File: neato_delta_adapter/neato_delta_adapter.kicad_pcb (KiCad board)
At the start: 2 copper layers, 43 x 21 mm, 11 parts, among them J1 JST PH2.0 B4B Vert, J2 JST PH2.0 B2B Vert, J3 JST PH B4B Vert, J4 JST PH2.0 B5B Vert, Q1 AS2302, U1 DNP LM2596

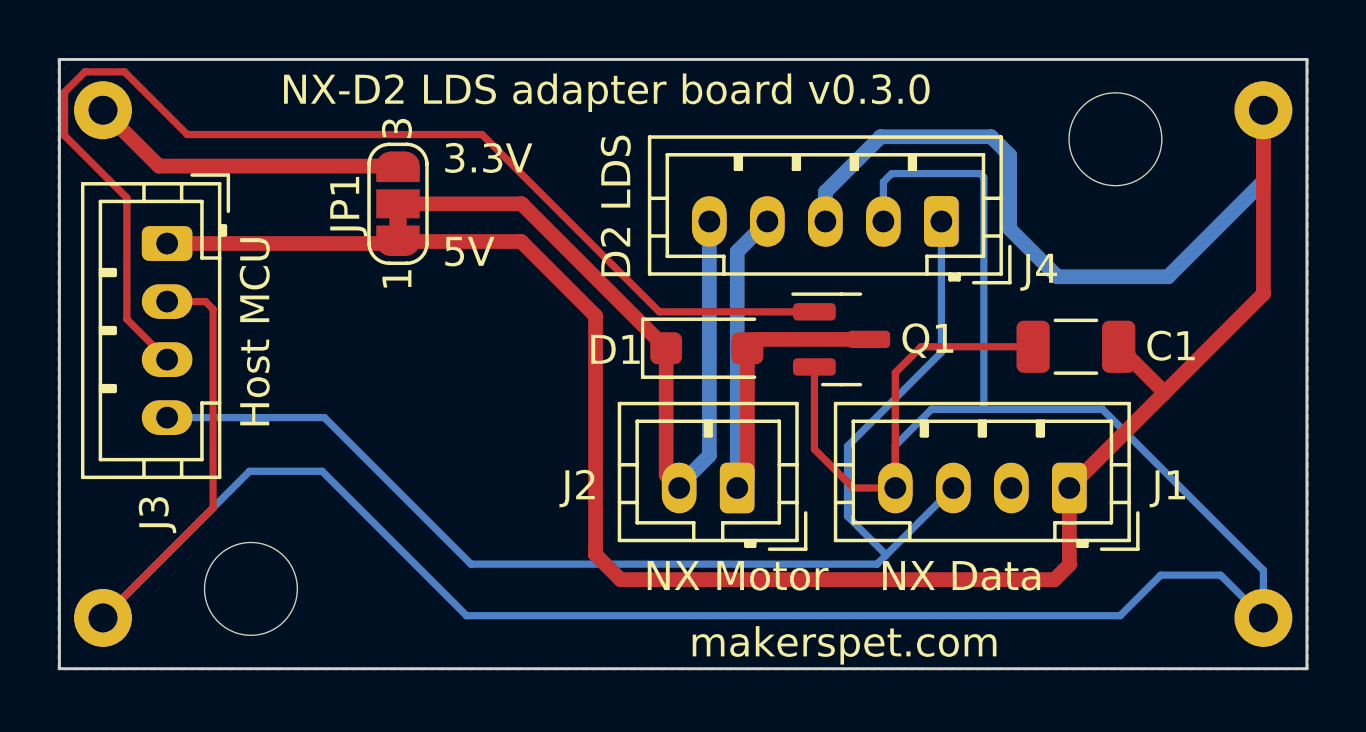
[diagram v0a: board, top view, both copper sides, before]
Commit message: Level shifter for Delta
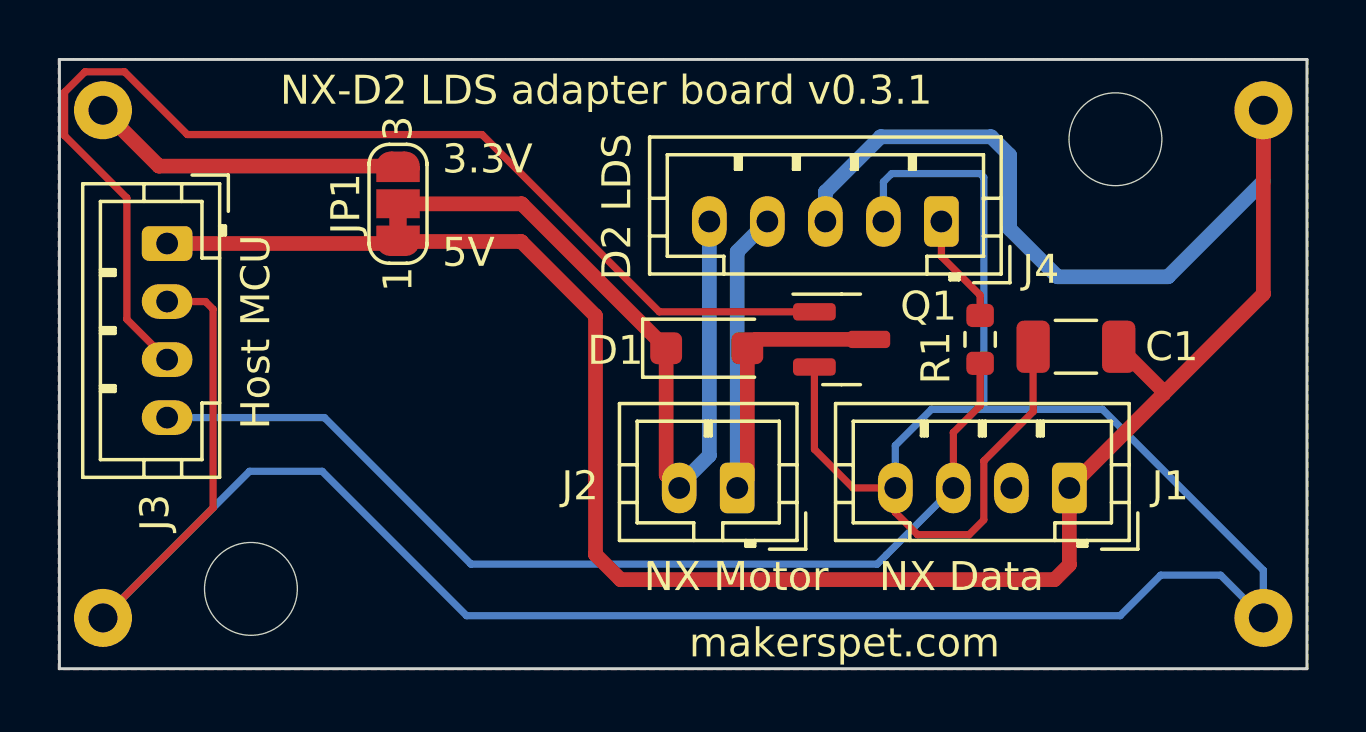
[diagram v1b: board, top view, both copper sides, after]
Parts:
- added R1: 10k, Resistor_SMD:R_0603_1608Metric, F.Cu at (110.2, 49.1)
- J4: value JST PH2.0 B5B Vert -> DNP JST PH2.0 B5B Vert
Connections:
- J4 pad 1: /TX -> Net-(J4-Pin_1)
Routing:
- net /TX: track 43.7 -> 35.0 mm
- net Net-(J4-Pin_1): track 0.00 -> 3.79 mm
- net GND: track 106.1 -> 108.1 mm
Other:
- board text added: "NX-D2 LDS adapter board v0.3.1"
- board text removed: "NX-D2 LDS adapter board v0.3.0"

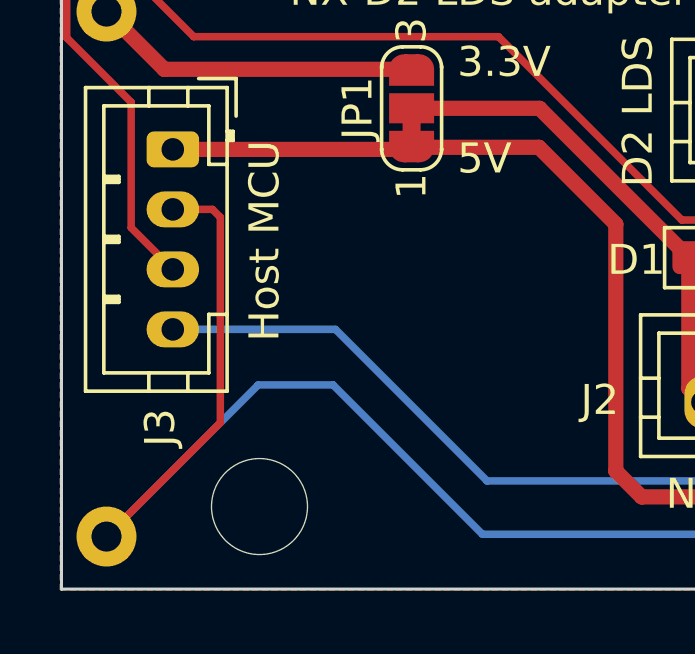
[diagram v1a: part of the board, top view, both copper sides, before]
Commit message: Delta motor enable pulldown
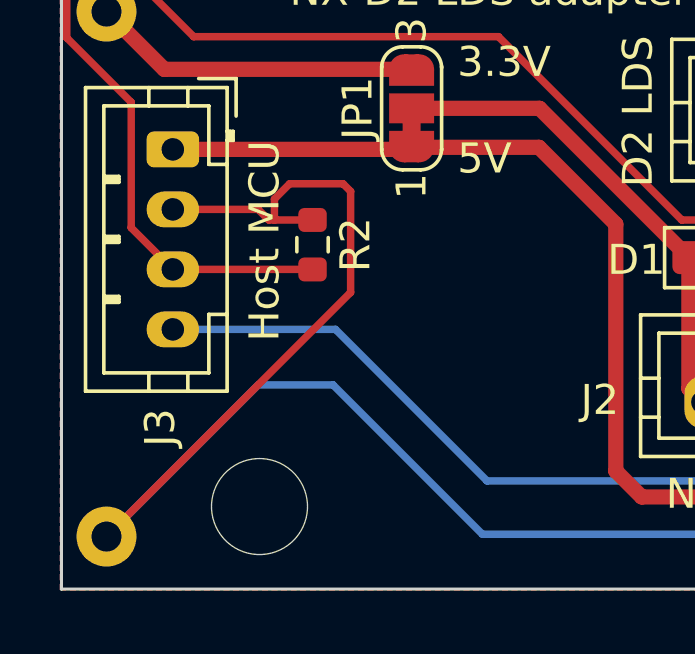
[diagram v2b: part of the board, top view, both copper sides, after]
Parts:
- added R2: 10k, Resistor_SMD:R_0603_1608Metric, F.Cu at (86.9, 49.0)
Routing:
- net GND: track 108.1 -> 117.5 mm
- net /MOT_EN: track 40.2 -> 44.9 mm
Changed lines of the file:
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@@
     (pad "" np_thru_hole circle (at 0 0) (size 3.2 3.2) (drill 3.2) (layers "*.Cu" "*.Mask"))
+  )
+  (footprint "Resistor_SMD:R_0603_1608Metric" (layer "F.Cu")
+    (at 86.868 49.022 -90)
+    (descr "Resistor SMD 0603 (1608 Metric), square (rectangular) end terminal, IPC_7351 nominal, (Body size source: IPC-SM-782 page 72, https://www.pcb-3d.com/wordpress/wp-content/uploads/ipc-sm-782a_amendment_1_and_2.pdf), generated with kicad-footprint-generator")
+    (tags "resistor")
+    (property "Sheetfile" "neato_delta_adapter.kicad_sch")
+    (property "Sheetname" "")
+    (property "ki_description" "Resistor, small US symbol")
+    (property "ki_keywords" "r resistor")
+    (attr smd)
+    (fp_text reference "R2" (at 0 -1.43 90) (layer "F.SilkS")
+        (effects (font (size 1 1) (thickness 0.15)))
+    )
+    (fp_text value "10k" (at 0 1.43 90) (layer "F.Fab") hide
+        (effects (font (size 1 1) (thickness 0.15)))
+    )
+    (fp_text user "${REFERENCE}" (at 0 0 90) (layer "F.Fab")
+        (effects (font (size 0.4 0.4) (thickness 0.06)))
+    )
+    (fp_line (start -0.237258 -0.5225) (end 0.237258 -0.5225)
+      (stroke (width 0.12) (type solid)) (layer "F.SilkS"))
+    (fp_line (start -0.237258 0.5225) (end 0.237258 0.5225)
+      (stroke (width 0.12) (type solid)) (layer "F.SilkS"))
+    (fp_line (start -1.48 -0.73) (end 1.48 -0.73)
+      (stroke (width 0.05) (type solid)) (layer "F.CrtYd"))
+    (fp_line (start -1.48 0.73) (end -1.48 -0.73)
+      (stroke (width 0.05) (type solid)) (layer "F.CrtYd"))
+    (fp_line (start 1.48 -0.73) (end 1.48 0.73)
+      (stroke (width 0.05) (type solid)) (layer "F.CrtYd"))
+    (fp_line (start 1.48 0.73) (end -1.48 0.73)
+      (stroke (width 0.05) (type solid)) (layer "F.CrtYd"))
+    (fp_line (start -0.8 -0.4125) (end 0.8 -0.4125)
+      (stroke (width 0.1) (type solid)) (layer "F.Fab"))
+    (fp_line (start -0.8 0.4125) (end -0.8 -0.4125)
+      (stroke (width 0.1) (type solid)) (layer "F.Fab"))
+    (fp_line (start 0.8 -0.4125) (end 0.8 0.4125)
+      (stroke (width 0.1) (type solid)) (layer "F.Fab"))
+    (fp_line (start 0.8 0.4125) (end -0.8 0.4125)
+      (stroke (width 0.1) (type solid)) (layer "F.Fab"))
+    (pad "1" smd roundrect (at -0.825 0 270) (size 0.8 0.95) (layers "F.Cu" "F.Paste" "F.Mask") (roundrect_rratio 0.25)
+      (net 5 "GND") (pintype "passive"))
+    (pad "2" smd roundrect (at 0.825 0 270) (size 0.8 0.95) (layers "F.Cu" "F.Paste" "F.Mask") (roundrect_rratio 0.25)
+      (net 7 "/MOT_EN") (pintype "passive"))
+    (model "${KICAD6_3DMODEL_DIR}/Resistor_SMD.3dshapes/R_0603_1608Metric.wrl"
+      (offset (xyz 0 0 0))
+      (scale (xyz 1 1 1))
+      (rotate (xyz 0 0 0))
+    )
   )
   (footprint "Makerspet:LM2596 Module" (layer "B.Cu")
@@
   (segment (start 108.077 55.88) (end 107.3122 55.1152) (width 0.25) (layer "F.Cu") (net 5))
   (segment (start 104.5233 50.099) (end 104.5233 52.9359) (width 0.25) (layer "F.Cu") (net 5))
+  (segment (start 85.598 48.197) (end 85.408 48.197) (width 0.25) (layer "F.Cu") (net 5))
+  (segment (start 88.138 47.244) (end 87.884 46.99) (width 0.25) (layer "F.Cu") (net 5))
   (segment (start 110.363 55.372) (end 109.855 55.88) (width 0.25) (layer "F.Cu") (net 5))
-  (segment (start 83.5312 47.8442) (end 82.211 47.8442) (width 0.25) (layer "F.Cu") (net 5))
+  (segment (start 80 58.75) (end 88.138 50.612) (width 0.25) (layer "F.Cu") (net 5))
   (segment (start 105.8584 54.271) (end 107.3122 54.271) (width 0.25) (layer "F.Cu") (net 5))
   (segment (start 109.855 55.88) (end 108.077 55.88) (width 0.25) (layer "F.Cu") (net 5))
-  (segment (start 83.7946 48.1076) (end 83.5312 47.8442) (width 0.25) (layer "F.Cu") (net 5))
+  (segment (start 86.106 46.99) (end 85.598 47.498) (width 0.25) (layer "F.Cu") (net 5))
+  (segment (start 85.598 47.498) (end 85.598 48.197) (width 0.25) (layer "F.Cu") (net 5))
   (segment (start 107.3122 55.1152) (end 107.3122 54.271) (width 0.25) (layer "F.Cu") (net 5))
-  (segment (start 80 58.75) (end 83.7946 54.9554) (width 0.25) (layer "F.Cu") (net 5))
+  (segment (start 86.868 48.197) (end 85.598 48.197) (width 0.25) (layer "F.Cu") (net 5))
+  (segment (start 88.138 50.612) (end 88.138 47.244) (width 0.25) (layer "F.Cu") (net 5))
   (segment (start 112.063 49.403) (end 112.063 51.64) (width 0.25) (layer "F.Cu") (net 5))
-  (segment (start 83.7946 54.9554) (end 83.7946 48.1076) (width 0.25) (layer "F.Cu") (net 5))
+  (segment (start 85.0552 47.8442) (end 82.211 47.8442) (width 0.25) (layer "F.Cu") (net 5))
+  (segment (start 87.884 46.99) (end 86.106 46.99) (width 0.25) (layer "F.Cu") (net 5))
   (segment (start 104.5233 52.9359) (end 105.8584 54.271) (width 0.25) (layer "F.Cu") (net 5))
   (segment (start 110.363 53.34) (end 110.363 55.372) (width 0.25) (layer "F.Cu") (net 5))
   (segment (start 112.063 51.64) (end 110.363 53.34) (width 0.25) (layer "F.Cu") (net 5))
+  (segment (start 85.408 48.197) (end 85.0552 47.8442) (width 0.25) (layer "F.Cu") (net 5))
   (segment (start 120 58.75) (end 120 57.1096) (width 0.25) (layer "B.Cu") (net 5))
   (segment (start 92.5322 58.674) (end 87.5538 53.6956) (width 0.25) (layer "B.Cu") (net 5))
@@
   (segment (start 99.8634 54.1876) (end 99.8634 54.271) (width 0.508) (layer "B.Cu") (net 6))
   (segment (start 78.675 40.6288) (end 78.675 42.1244) (width 0.25) (layer "F.Cu") (net 7))
+  (segment (start 86.8652 49.8442) (end 86.868 49.847) (width 0.25) (layer "F.Cu") (net 7))
   (segment (start 93.0656 42.0878) (end 82.9056 42.0878) (width 0.25) (layer "F.Cu") (net 7))
   (segment (start 78.675 42.1244) (end 80.8228 44.2722) (width 0.25) (layer "F.Cu") (net 7))
@@
   (segment (start 80.8228 44.2722) (end 80.8228 48.456) (width 0.25) (layer "F.Cu") (net 7))
   (segment (start 80.7428 39.925) (end 79.3788 39.925) (width 0.25) (layer "F.Cu") (net 7))
+  (segment (start 82.211 49.8442) (end 86.8652 49.8442) (width 0.25) (layer "F.Cu") (net 7))
   (segment (start 81.9254 43.1754) (end 80 41.25) (width 0.508) (layer "F.Cu") (net 8))
   (segment (start 90.17 43.1754) (end 81.9254 43.1754) (width 0.508) (layer "F.Cu") (net 8))
